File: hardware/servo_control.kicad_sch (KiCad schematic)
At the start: 0 parts

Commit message: Schematic first draft
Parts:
- added J10, J11, J12, J9: Conn_01x03, symbol Connector_Generic:Conn_01x03
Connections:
- new net GND: J10.3 (Pin_3), J11.3 (Pin_3), J12.3 (Pin_3), J9.3 (Pin_3)
- new net SERVO_DATA: J10.2 (Pin_2), J11.2 (Pin_2), J12.2 (Pin_2), J9.2 (Pin_2)
- new net V_BATT: J10.1 (Pin_1), J11.1 (Pin_1), J12.1 (Pin_1), J9.1 (Pin_1)

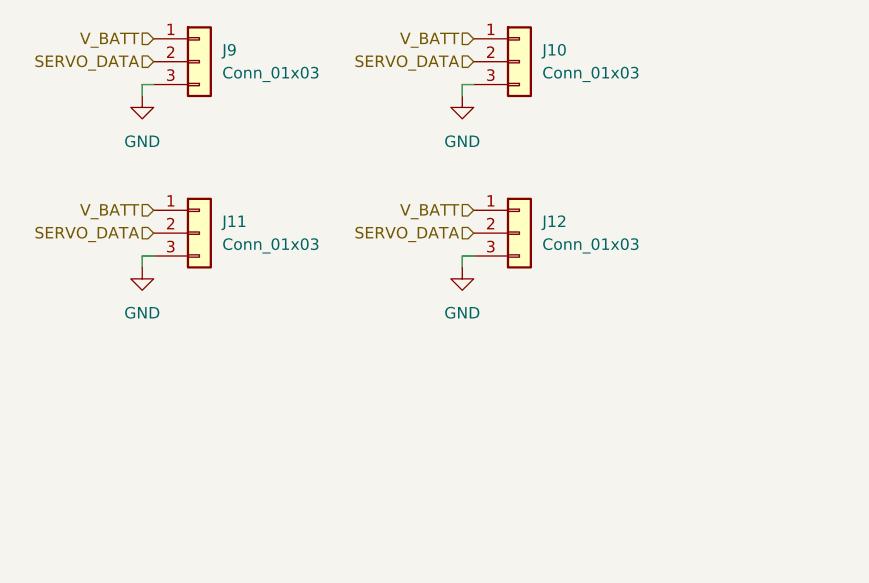
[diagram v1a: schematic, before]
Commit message: Annotating schematic
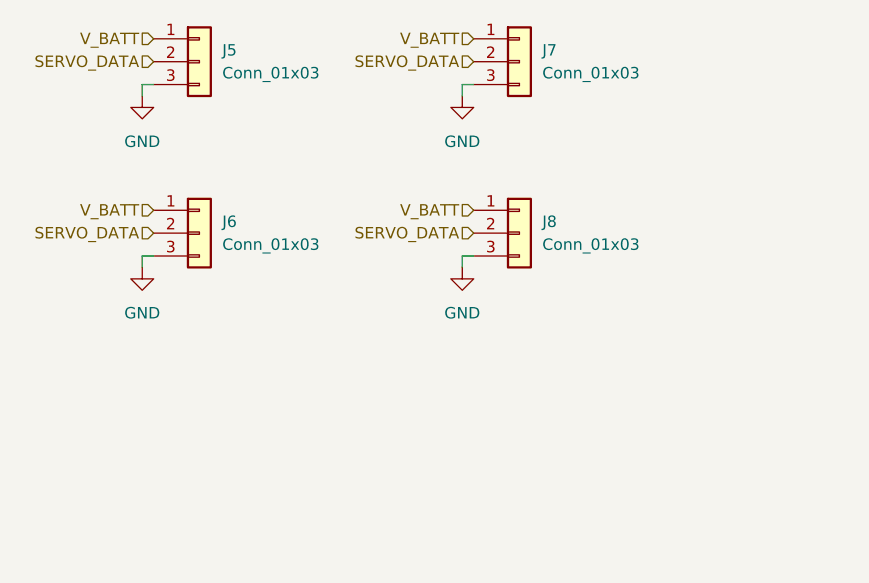
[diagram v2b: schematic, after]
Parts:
- renumbered J9 to J5, J11 to J6, J10 to J7, J12 to J8
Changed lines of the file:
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@@
 		(dnp no)
 		(fields_autoplaced yes)
-		(property "Reference" "#PWR0102"
+		(property "Reference" "#PWR056"
 			(at 148.59 85.09 0)
 			(effects
@@
 			(project "chromapi_motherboard_v1"
 				(path "/d1a31f26-03e0-43e1-89c1-031fe31befc5/65907df6-508b-450c-8c31-d637ad608dec"
-					(reference "#PWR0102")
+					(reference "#PWR056")
 					(unit 1)
 				)
@@
 		(dnp no)
 		(fields_autoplaced yes)
-		(property "Reference" "#PWR0101"
+		(property "Reference" "#PWR054"
 			(at 113.03 85.09 0)
 			(effects
@@
 			(project ""
 				(path "/d1a31f26-03e0-43e1-89c1-031fe31befc5/65907df6-508b-450c-8c31-d637ad608dec"
-					(reference "#PWR0101")
+					(reference "#PWR054")
 					(unit 1)
 				)
@@
 		(dnp no)
 		(fields_autoplaced yes)
-		(property "Reference" "J11"
+		(property "Reference" "J6"
 			(at 121.92 92.7099 0)
 			(effects
@@
 			(project "chromapi_motherboard_v1"
 				(path "/d1a31f26-03e0-43e1-89c1-031fe31befc5/65907df6-508b-450c-8c31-d637ad608dec"
-					(reference "J11")
+					(reference "J6")
 					(unit 1)
 				)
@@
 		(dnp no)
 		(fields_autoplaced yes)
-		(property "Reference" "#PWR0104"
+		(property "Reference" "#PWR057"
 			(at 148.59 104.14 0)
 			(effects
@@
 			(project "chromapi_motherboard_v1"
 				(path "/d1a31f26-03e0-43e1-89c1-031fe31befc5/65907df6-508b-450c-8c31-d637ad608dec"
-					(reference "#PWR0104")
+					(reference "#PWR057")
 					(unit 1)
 				)
@@
 		(dnp no)
 		(fields_autoplaced yes)
-		(property "Reference" "J12"
+		(property "Reference" "J8"
 			(at 157.48 92.7099 0)
 			(effects
@@
 			(project "chromapi_motherboard_v1"
 				(path "/d1a31f26-03e0-43e1-89c1-031fe31befc5/65907df6-508b-450c-8c31-d637ad608dec"
-					(reference "J12")
+					(reference "J8")
 					(unit 1)
 				)
@@
 		(dnp no)
 		(fields_autoplaced yes)
-		(property "Reference" "#PWR0103"
+		(property "Reference" "#PWR055"
 			(at 113.03 104.14 0)
 			(effects
@@
 			(project "chromapi_motherboard_v1"
 				(path "/d1a31f26-03e0-43e1-89c1-031fe31befc5/65907df6-508b-450c-8c31-d637ad608dec"
-					(reference "#PWR0103")
+					(reference "#PWR055")
 					(unit 1)
 				)
@@
 		(dnp no)
 		(fields_autoplaced yes)
-		(property "Reference" "J10"
+		(property "Reference" "J7"
 			(at 157.48 73.6599 0)
 			(effects
@@
 			(project "chromapi_motherboard_v1"
 				(path "/d1a31f26-03e0-43e1-89c1-031fe31befc5/65907df6-508b-450c-8c31-d637ad608dec"
-					(reference "J10")
+					(reference "J7")
 					(unit 1)
 				)
@@
 		(dnp no)
 		(fields_autoplaced yes)
-		(property "Reference" "J9"
+		(property "Reference" "J5"
 			(at 121.92 73.6599 0)
 			(effects
@@
 			(project ""
 				(path "/d1a31f26-03e0-43e1-89c1-031fe31befc5/65907df6-508b-450c-8c31-d637ad608dec"
-					(reference "J9")
-					(unit 1)
-				)
+					(reference "J5")
+					(unit 1)
+				)

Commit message: Updating schematic
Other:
- moved on the sheet: J5, J6, J7, J8
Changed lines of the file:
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@@
 		(comment 1 "Ousmane THIONGANE")
 	)
+	(text_box "Servomotor connectors"
+		(exclude_from_sim no)
+		(at 104.14 72.39 0)
+		(size 85.09 58.42)
+		(margins 0.9525 0.9525 0.9525 0.9525)
+		(stroke
+			(width 0)
+			(type dash)
+		)
+		(fill
+			(type none)
+		)
+		(effects
+			(font
+				(size 1.27 1.27)
+			)
+			(justify left top)
+		)
+	)
 	(wire
 		(pts
-			(xy 148.59 96.52) (xy 148.59 97.79)
+			(xy 161.29 113.03) (xy 161.29 114.3)
 		)
 		(stroke
@@
 	(wire
 		(pts
-			(xy 149.86 77.47) (xy 148.59 77.47)
+			(xy 162.56 93.98) (xy 161.29 93.98)
 		)
 		(stroke
@@
 	(wire
 		(pts
-			(xy 113.03 77.47) (xy 113.03 78.74)
+			(xy 125.73 93.98) (xy 125.73 95.25)
 		)
 		(stroke
@@
 	(wire
 		(pts
-			(xy 114.3 96.52) (xy 113.03 96.52)
+			(xy 127 113.03) (xy 125.73 113.03)
 		)
 		(stroke
@@
 	(wire
 		(pts
-			(xy 149.86 96.52) (xy 148.59 96.52)
+			(xy 162.56 113.03) (xy 161.29 113.03)
 		)
 		(stroke
@@
 	(wire
 		(pts
-			(xy 114.3 77.47) (xy 113.03 77.47)
+			(xy 127 93.98) (xy 125.73 93.98)
 		)
 		(stroke
@@
 	(wire
 		(pts
-			(xy 113.03 96.52) (xy 113.03 97.79)
+			(xy 125.73 113.03) (xy 125.73 114.3)
 		)
 		(stroke
@@
 	(wire
 		(pts
-			(xy 148.59 77.47) (xy 148.59 78.74)
+			(xy 161.29 93.98) (xy 161.29 95.25)
 		)
 		(stroke
@@
 	(hierarchical_label "SERVO_DATA"
 		(shape input)
-		(at 114.3 93.98 180)
+		(at 127 110.49 180)
 		(effects
 			(font
@@
 	(hierarchical_label "SERVO_DATA"
 		(shape input)
-		(at 149.86 74.93 180)
+		(at 162.56 91.44 180)
 		(effects
 			(font
@@
 	(hierarchical_label "SERVO_DATA"
 		(shape input)
-		(at 114.3 74.93 180)
+		(at 127 91.44 180)
 		(effects
 			(font
@@
 	(hierarchical_label "V_BATT"
 		(shape input)
-		(at 149.86 72.39 180)
+		(at 162.56 88.9 180)
 		(effects
 			(font
@@
 	(hierarchical_label "SERVO_DATA"
 		(shape input)
-		(at 149.86 93.98 180)
+		(at 162.56 110.49 180)
 		(effects
 			(font
@@
 	(hierarchical_label "V_BATT"
 		(shape input)
-		(at 114.3 91.44 180)
+		(at 127 107.95 180)
 		(effects
 			(font
@@
 	(hierarchical_label "V_BATT"
 		(shape input)
-		(at 114.3 72.39 180)
+		(at 127 88.9 180)
 		(effects
 			(font
@@
 	(hierarchical_label "V_BATT"
 		(shape input)
-		(at 149.86 91.44 180)
+		(at 162.56 107.95 180)
 		(effects
 			(font
@@
 	(symbol
 		(lib_id "power:GND")
-		(at 148.59 78.74 0)
+		(at 161.29 95.25 0)
 		(unit 1)
 		(exclude_from_sim no)
@@
 		(fields_autoplaced yes)
 		(property "Reference" "#PWR056"
-			(at 148.59 85.09 0)
+			(at 161.29 101.6 0)
 			(effects
 				(font
@@
 		)
 		(property "Value" "GND"
-			(at 148.59 83.82 0)
+			(at 161.29 100.33 0)
 			(effects
 				(font
@@
 		)
 		(property "Footprint" ""
-			(at 148.59 78.74 0)
+			(at 161.29 95.25 0)
 			(effects
 				(font
@@
 		)
 		(property "Datasheet" ""
-			(at 148.59 78.74 0)
+			(at 161.29 95.25 0)
 			(effects
 				(font
@@
 		)
 		(property "Description" "Power symbol creates a global label with name \"GND\" , ground"
-			(at 148.59 78.74 0)
+			(at 161.29 95.25 0)
 			(effects
 				(font
@@
 	(symbol
 		(lib_id "power:GND")
-		(at 113.03 78.74 0)
+		(at 125.73 95.25 0)
 		(unit 1)
 		(exclude_from_sim no)
@@
 		(fields_autoplaced yes)
 		(property "Reference" "#PWR054"
-			(at 113.03 85.09 0)
+			(at 125.73 101.6 0)
 			(effects
 				(font
@@
 		)
 		(property "Value" "GND"
-			(at 113.03 83.82 0)
+			(at 125.73 100.33 0)
 			(effects
 				(font
@@
 		)
 		(property "Footprint" ""
-			(at 113.03 78.74 0)
+			(at 125.73 95.25 0)
 			(effects
 				(font
@@
 		)
 		(property "Datasheet" ""
-			(at 113.03 78.74 0)
+			(at 125.73 95.25 0)
 			(effects
 				(font
@@
 		)
 		(property "Description" "Power symbol creates a global label with name \"GND\" , ground"
-			(at 113.03 78.74 0)
+			(at 125.73 95.25 0)
 			(effects
 				(font
@@
 	(symbol
 		(lib_id "Connector_Generic:Conn_01x03")
-		(at 119.38 93.98 0)
+		(at 132.08 110.49 0)
 		(unit 1)
 		(exclude_from_sim no)
@@
 		(fields_autoplaced yes)
 		(property "Reference" "J6"
-			(at 121.92 92.7099 0)
+			(at 134.62 109.2199 0)
 			(effects
 				(font
@@
 		)
 		(property "Value" "Conn_01x03"
-			(at 121.92 95.2499 0)
+			(at 134.62 111.7599 0)
 			(effects
 				(font
@@
 		)
 		(property "Footprint" ""
-			(at 119.38 93.98 0)
+			(at 132.08 110.49 0)
 			(effects
 				(font
@@
 		)
 		(property "Datasheet" "~"
-			(at 119.38 93.98 0)
+			(at 132.08 110.49 0)
 			(effects
 				(font
@@
 		)
 		(property "Description" "Generic connector, single row, 01x03, script generated (kicad-library-utils/schlib/autogen/connector/)"
-			(at 119.38 93.98 0)
+			(at 132.08 110.49 0)
 			(effects
 				(font
@@
 	(symbol
 		(lib_id "power:GND")
-		(at 148.59 97.79 0)
+		(at 161.29 114.3 0)
 		(unit 1)
 		(exclude_from_sim no)
@@
 		(fields_autoplaced yes)
 		(property "Reference" "#PWR057"
-			(at 148.59 104.14 0)
+			(at 161.29 120.65 0)
 			(effects
 				(font
@@
 		)
 		(property "Value" "GND"
-			(at 148.59 102.87 0)
+			(at 161.29 119.38 0)
 			(effects
 				(font
@@
 		)
 		(property "Footprint" ""
-			(at 148.59 97.79 0)
+			(at 161.29 114.3 0)
 			(effects
 				(font
@@
 		)
 		(property "Datasheet" ""
-			(at 148.59 97.79 0)
+			(at 161.29 114.3 0)
 			(effects
 				(font
@@
 		)
 		(property "Description" "Power symbol creates a global label with name \"GND\" , ground"
-			(at 148.59 97.79 0)
+			(at 161.29 114.3 0)
 			(effects
 				(font
@@
 	(symbol
 		(lib_id "Connector_Generic:Conn_01x03")
-		(at 154.94 93.98 0)
+		(at 167.64 110.49 0)
 		(unit 1)
 		(exclude_from_sim no)
@@
 		(fields_autoplaced yes)
 		(property "Reference" "J8"
-			(at 157.48 92.7099 0)
+			(at 170.18 109.2199 0)
 			(effects
 				(font
@@
 		)
 		(property "Value" "Conn_01x03"
-			(at 157.48 95.2499 0)
+			(at 170.18 111.7599 0)
 			(effects
 				(font
@@
 		)
 		(property "Footprint" ""
-			(at 154.94 93.98 0)
+			(at 167.64 110.49 0)
 			(effects
 				(font
@@
 		)
 		(property "Datasheet" "~"
-			(at 154.94 93.98 0)
+			(at 167.64 110.49 0)
 			(effects
 				(font
@@
 		)
 		(property "Description" "Generic connector, single row, 01x03, script generated (kicad-library-utils/schlib/autogen/connector/)"
-			(at 154.94 93.98 0)
+			(at 167.64 110.49 0)
 			(effects
 				(font
@@
 	(symbol
 		(lib_id "power:GND")
-		(at 113.03 97.79 0)
+		(at 125.73 114.3 0)
 		(unit 1)
 		(exclude_from_sim no)
@@
 		(fields_autoplaced yes)
 		(property "Reference" "#PWR055"
-			(at 113.03 104.14 0)
+			(at 125.73 120.65 0)
 			(effects
 				(font
@@
 		)
 		(property "Value" "GND"
-			(at 113.03 102.87 0)
+			(at 125.73 119.38 0)
 			(effects
 				(font
@@
 		)
 		(property "Footprint" ""
-			(at 113.03 97.79 0)
+			(at 125.73 114.3 0)
 			(effects
 				(font
@@
 		)
 		(property "Datasheet" ""
-			(at 113.03 97.79 0)
+			(at 125.73 114.3 0)
 			(effects
 				(font
@@
 		)
 		(property "Description" "Power symbol creates a global label with name \"GND\" , ground"
-			(at 113.03 97.79 0)
+			(at 125.73 114.3 0)
 			(effects
 				(font
@@
 	(symbol
 		(lib_id "Connector_Generic:Conn_01x03")
-		(at 154.94 74.93 0)
+		(at 167.64 91.44 0)
 		(unit 1)
 		(exclude_from_sim no)
@@
 		(fields_autoplaced yes)
 		(property "Reference" "J7"
-			(at 157.48 73.6599 0)
+			(at 170.18 90.1699 0)
 			(effects
 				(font
@@
 		)
 		(property "Value" "Conn_01x03"
-			(at 157.48 76.1999 0)
+			(at 170.18 92.7099 0)
 			(effects
 				(font
@@
 		)
 		(property "Footprint" ""
-			(at 154.94 74.93 0)
+			(at 167.64 91.44 0)
 			(effects
 				(font
@@
 		)
 		(property "Datasheet" "~"
-			(at 154.94 74.93 0)
+			(at 167.64 91.44 0)
 			(effects
 				(font
@@
 		)
 		(property "Description" "Generic connector, single row, 01x03, script generated (kicad-library-utils/schlib/autogen/connector/)"
-			(at 154.94 74.93 0)
+			(at 167.64 91.44 0)
 			(effects
 				(font
@@
 	(symbol
 		(lib_id "Connector_Generic:Conn_01x03")
-		(at 119.38 74.93 0)
+		(at 132.08 91.44 0)
 		(unit 1)
 		(exclude_from_sim no)
@@
 		(fields_autoplaced yes)
 		(property "Reference" "J5"
-			(at 121.92 73.6599 0)
+			(at 134.62 90.1699 0)
 			(effects
 				(font
@@
 		)
 		(property "Value" "Conn_01x03"
-			(at 121.92 76.1999 0)
+			(at 134.62 92.7099 0)
 			(effects
 				(font
@@
 		)
 		(property "Footprint" ""
-			(at 119.38 74.93 0)
+			(at 132.08 91.44 0)
 			(effects
 				(font
@@
 		)
 		(property "Datasheet" "~"
-			(at 119.38 74.93 0)
+			(at 132.08 91.44 0)
 			(effects
 				(font
@@
 		)
 		(property "Description" "Generic connector, single row, 01x03, script generated (kicad-library-utils/schlib/autogen/connector/)"
-			(at 119.38 74.93 0)
+			(at 132.08 91.44 0)
 			(effects
 				(font
